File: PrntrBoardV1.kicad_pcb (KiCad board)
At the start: 4 copper layers, 99 x 99 mm, 221 parts, among them J1 EXT 5V, J10 Probe, J11 Extruder Heater, J12 Stepper, J13 Thermistor, J14 Max, J15 Min, J16 Max, J17 Min, J18 Max, J19 Min, J2 Bed Heater, J20 Stepper, J21 Stepper, J22 Stepper, J23 Stepper, J24 Probe, J25 Extruder Heater, J26 Stepper, J27 Thermistor, J28 Thermistor, J29 12-24V, J3 Z Probe, J30 Ext Motor Clock, J4 E0 Cool, J5 E0 Part, J6 E1 Cool, J7 E1 Part, J8 Always On Fan 1, J9 Always On Fan 2, U1 4078, U11 NUCLEO-64, U2 74HCT02, U3 74LVC125, U4 TMC5130, U5 TMC5130, U6 TMC5130, U7 TMC5130, U8 TMC5130

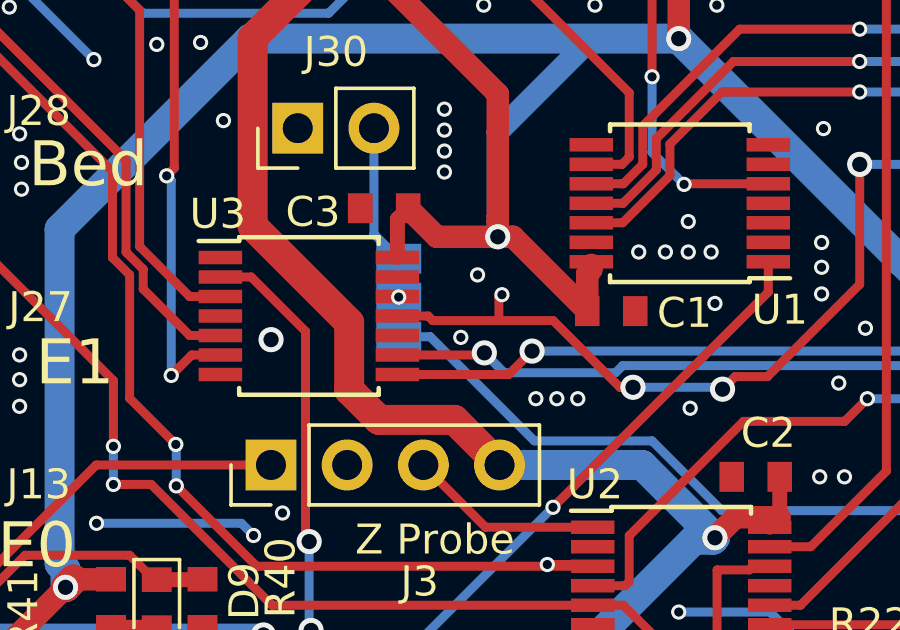
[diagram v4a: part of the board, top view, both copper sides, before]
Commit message: Some useless changes, I'll remove the SD_MODE wire soon.
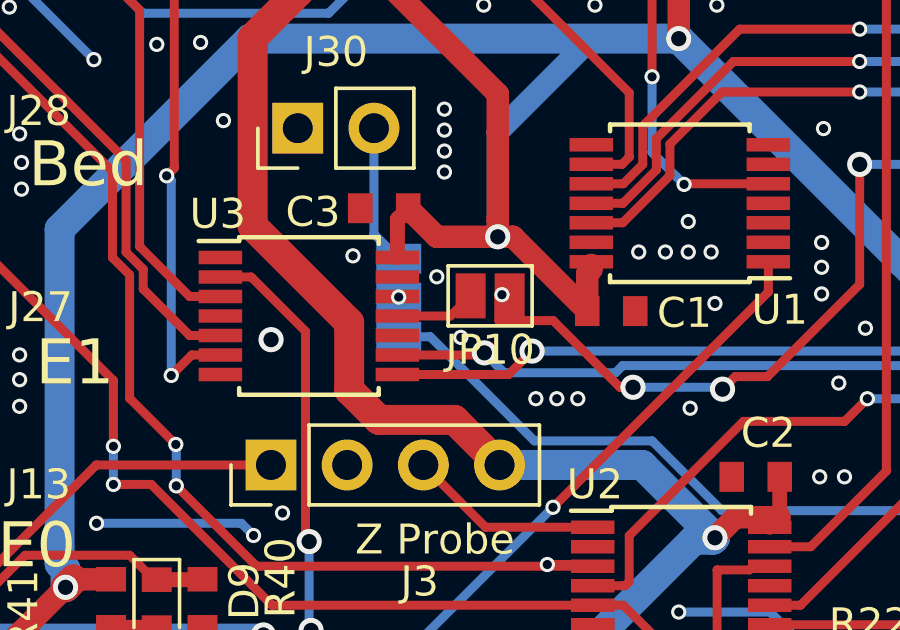
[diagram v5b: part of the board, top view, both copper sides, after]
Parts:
- added JP10: Motor Clock Enable, Jumper:SolderJumper-2_P1.3mm_Open_Pad1.0x1.5mm, F.Cu at (53.4, 75.1)
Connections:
- U3 pad 11: /MotorControl/E0/CLOCK -> Net-(JP10-Pad2)
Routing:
- net /MotorControl/E0/CLOCK: track 207.4 -> 203.9 mm
- net Net-(JP10-Pad2): track 0.00 -> 2.72 mm
- net GND: vias 681 -> 682
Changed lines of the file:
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@@
     (tracks 2655)
     (zones 0)
-    (modules 221)
-    (nets 208)
+    (modules 222)
+    (nets 209)
   )
   (page A4)
@@
   (net 206 "/MotorControl/Z Motors/Motor1/MOTB1")
   (net 207 "Net-(JP8-Pad2)")
+  (net 208 "Net-(JP10-Pad2)")
   (net_class Default "This is the default net class."
     (clearance 0.1524)
@@
     (add_net "Net-(J3-Pad1)")
     (add_net "Net-(J30-Pad2)")
+    (add_net "Net-(JP10-Pad2)")
     (add_net "Net-(JP2-Pad1)")
     (add_net "Net-(JP8-Pad2)")
@@
     (add_net /5V)
   )
+  (module Jumper:SolderJumper-2_P1.3mm_Open_Pad1.0x1.5mm (layer F.Cu)
+    (at 53.4035 75.1205 180)
+    (descr "SMD Solder Jumper, 1x1.5mm Pads, 0.3mm gap, open")
+    (tags "solder jumper open")
+    (attr virtual)
+    (fp_text reference JP10 (at 0 -1.8 180) (layer F.SilkS)
+      (effects (font (size 1 1) (thickness 0.15)))
+    )
+    (fp_text value "Motor Clock Enable" (at 0 1.9 180) (layer F.Fab)
+      (effects (font (size 1 1) (thickness 0.15)))
+    )
+    (fp_line (start -1.4 1) (end -1.4 -1) (layer F.SilkS) (width 0.12))
+    (fp_line (start 1.4 1) (end -1.4 1) (layer F.SilkS) (width 0.12))
+    (fp_line (start 1.4 -1) (end 1.4 1) (layer F.SilkS) (width 0.12))
+    (fp_line (start -1.4 -1) (end 1.4 -1) (layer F.SilkS) (width 0.12))
+    (fp_line (start -1.65 -1.25) (end 1.65 -1.25) (layer F.CrtYd) (width 0.05))
+    (fp_line (start -1.65 -1.25) (end -1.65 1.25) (layer F.CrtYd) (width 0.05))
+    (fp_line (start 1.65 1.25) (end 1.65 -1.25) (layer F.CrtYd) (width 0.05))
+    (fp_line (start 1.65 1.25) (end -1.65 1.25) (layer F.CrtYd) (width 0.05))
+    (pad 2 smd rect (at 0.65 0 180) (size 1 1.5) (layers F.Cu F.Mask)
+      (net 208 "Net-(JP10-Pad2)"))
+    (pad 1 smd rect (at -0.65 0 180) (size 1 1.5) (layers F.Cu F.Mask)
+      (net 125 /MotorControl/E0/CLOCK))
+  )
   (module Resistor_SMD:R_0603_1608Metric (layer F.Cu)
     (at 66.0145 87.4395 180)
@@
       (net 126 /MOT_CLOCK))
     (pad 11 smd rect (at 2.95 0) (size 1.45 0.45) (layers F.Cu F.Paste F.Mask)
-      (net 125 /MotorControl/E0/CLOCK))
+      (net 208 "Net-(JP10-Pad2)"))
     (pad 10 smd rect (at 2.95 0.65) (size 1.45 0.45) (layers F.Cu F.Paste F.Mask)
       (net 8 GND))
@@
   (via (at 39.243 36.449) (size 0.508) (drill 0.3048) (layers F.Cu B.Cu) (net 8))
   (via (at 40.005 37.338) (size 0.508) (drill 0.3048) (layers F.Cu B.Cu) (net 8))
-  (via (at 52.9844 74.422) (size 0.508) (drill 0.3048) (layers F.Cu B.Cu) (net 8))
   (via (at 52.4256 76.5048) (size 0.508) (drill 0.3048) (layers F.Cu B.Cu) (net 8))
   (via (at 64.516 69.5452) (size 0.508) (drill 0.3048) (layers F.Cu B.Cu) (net 8))
@@
   (via (at 67.8815 86.868) (size 0.508) (drill 0.3048) (layers F.Cu B.Cu) (net 8))
   (via (at 64.9605 90.1065) (size 0.508) (drill 0.3048) (layers F.Cu B.Cu) (net 8))
+  (via (at 51.6255 74.4855) (size 0.508) (drill 0.3048) (layers F.Cu B.Cu) (net 8))
+  (via (at 48.8315 73.787) (size 0.508) (drill 0.3048) (layers F.Cu B.Cu) (net 8))
   (segment (start 73.364029 28.9306) (end 72.794629 29.5) (width 0.5) (layer F.Cu) (net 9))
   (segment (start 75.7653 28.9306) (end 74.5 28.9306) (width 0.5) (layer F.Cu) (net 9))
@@
   (segment (start 107.394322 74.669788) (end 107.711822 74.352288) (width 0.3) (layer B.Cu) (net 125))
   (segment (start 109.03175 61.646687) (end 109.03175 56.99575) (width 0.3) (layer B.Cu) (net 125))
-  (segment (start 51.337901 75.7929) (end 51.491001 75.946) (width 0.3) (layer F.Cu) (net 125))
-  (segment (start 50.312901 75.7929) (end 51.337901 75.7929) (width 0.3) (layer F.Cu) (net 125))
   (via (at 58.166 78.1685) (size 0.8382) (drill 0.508) (layers F.Cu B.Cu) (net 125))
   (segment (start 57.727678 78.1685) (end 58.166 78.1685) (width 0.3) (layer F.Cu) (net 125))
@@
   (segment (start 107.711822 74.352288) (end 107.711822 67.945) (width 0.3) (layer B.Cu) (net 125))
   (segment (start 53.6956 75.184) (end 53.7972 75.0824) (width 0.3) (layer F.Cu) (net 125))
-  (segment (start 51.491001 75.946) (end 53.6956 75.946) (width 0.3) (layer F.Cu) (net 125))
   (via (at 53.7972 75.0824) (size 0.508) (drill 0.3048) (layers F.Cu B.Cu) (net 125))
   (segment (start 53.6956 75.946) (end 53.6956 75.184) (width 0.3) (layer F.Cu) (net 125))
@@
   (segment (start 48.314799 38.978727) (end 49.659427 37.634099) (width 0.5) (layer In1.Cu) (net 207))
   (segment (start 49.659427 37.634099) (end 54.163073 37.634099) (width 0.5) (layer In1.Cu) (net 207))
+  (segment (start 52.0811 75.7929) (end 52.7535 75.1205) (width 0.3) (layer F.Cu) (net 208))
+  (segment (start 50.312901 75.7929) (end 52.0811 75.7929) (width 0.3) (layer F.Cu) (net 208))
   (zone (net 8) (net_name GND) (layer F.Cu) (hatch edge 0.508)
     (connect_pads (clearance 0.1524))

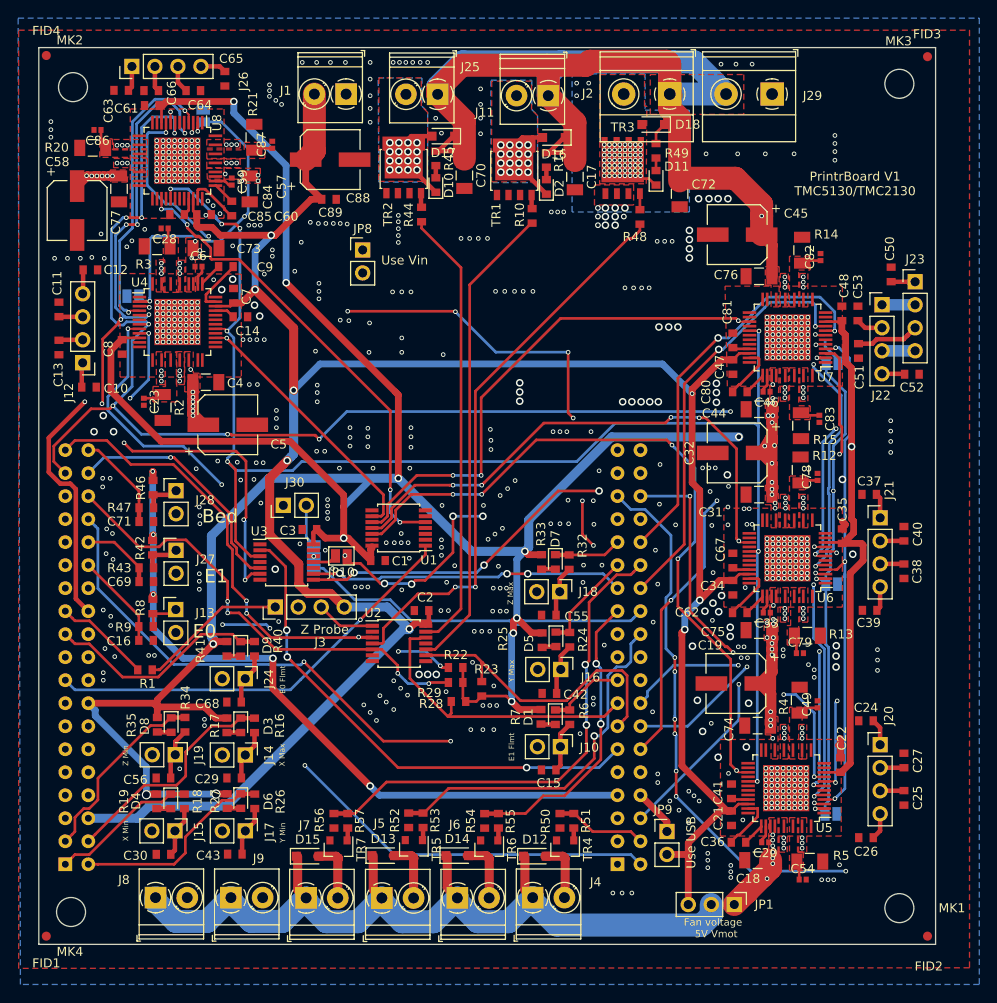
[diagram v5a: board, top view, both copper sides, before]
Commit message: Removed SD_MODE wire. Added motor clock oscillator. Wired the clock on the internal layer to reduce EMI.
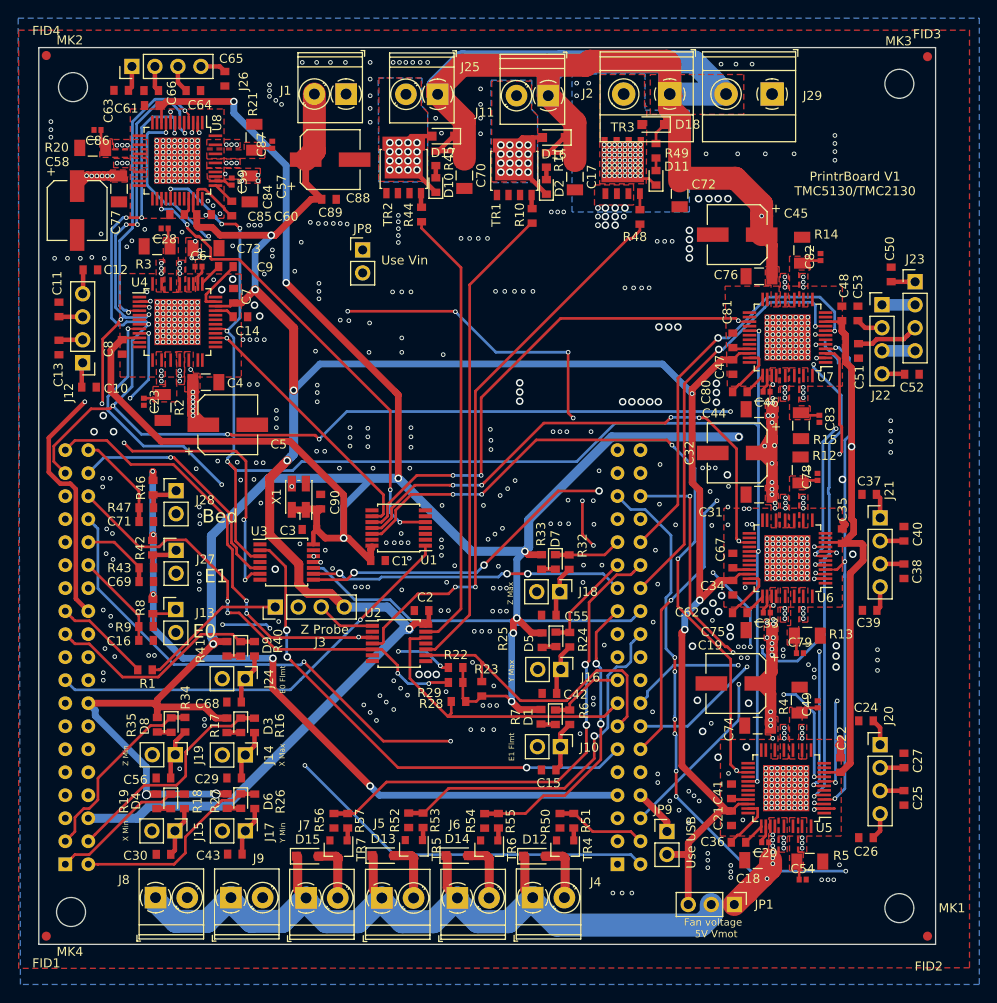
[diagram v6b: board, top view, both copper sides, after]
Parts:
- removed J30: Ext Motor Clock, Connector_PinHeader_2.54mm:PinHeader_1x02_P2.54mm_Vertical
- removed JP10: Motor Clock Enable, Jumper:SolderJumper-2_P1.3mm_Open_Pad1.0x1.5mm
- removed JP2: Motor Clock Select, Jumper:SolderJumper-3_P1.3mm_Open_Pad1.0x1.5mm
- removed JP3, JP4, JP5, JP6, JP7: Clock Disable, Jumper:SolderJumper-2_P1.3mm_Open_Pad1.0x1.5mm
- added C90: 0.1uF, Capacitor_SMD:C_0603_1608Metric, F.Cu at (51.1, 69.1)
- added X1: 16MHz, Oscillator:Oscillator_SMD_EuroQuartz_XO32-4Pin_3.2x2.5mm_HandSoldering, F.Cu at (48.7, 68.6)
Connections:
- U3 pad 11: Net-(JP10-Pad2) -> /MotorControl/E0/CLOCK
- U3 pad 12: /MOT_CLOCK -> Net-(U3-Pad12)
- U4 pad 11: GND -> Net-(U4-Pad11)
- U5 pad 11: GND -> Net-(U5-Pad11)
- U6 pad 11: GND -> Net-(U6-Pad11)
- U7 pad 11: GND -> Net-(U7-Pad11)
- U8 pad 11: GND -> Net-(U8-Pad11)
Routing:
- net /MotorControl/E0/CLOCK: track 203.9 -> 225.1 mm, vias 12 -> 6
- net /MotorControl/E0/MOSI: track 208.1 -> 218.9 mm, vias 15 -> 16
- net Net-(U3-Pad12): track 0.00 -> 8.73 mm, vias 0 -> 2
- net /3.3V: track 367.5 -> 373.2 mm
- net Net-(J30-Pad2): track 4.69 -> 0.00 mm
- net Net-(JP10-Pad2): track 2.72 -> 0.00 mm
- net /MOT_CLOCK: track 0.02 -> 0.00 mm, vias 1 -> 0
- net GND: vias 682 -> 680

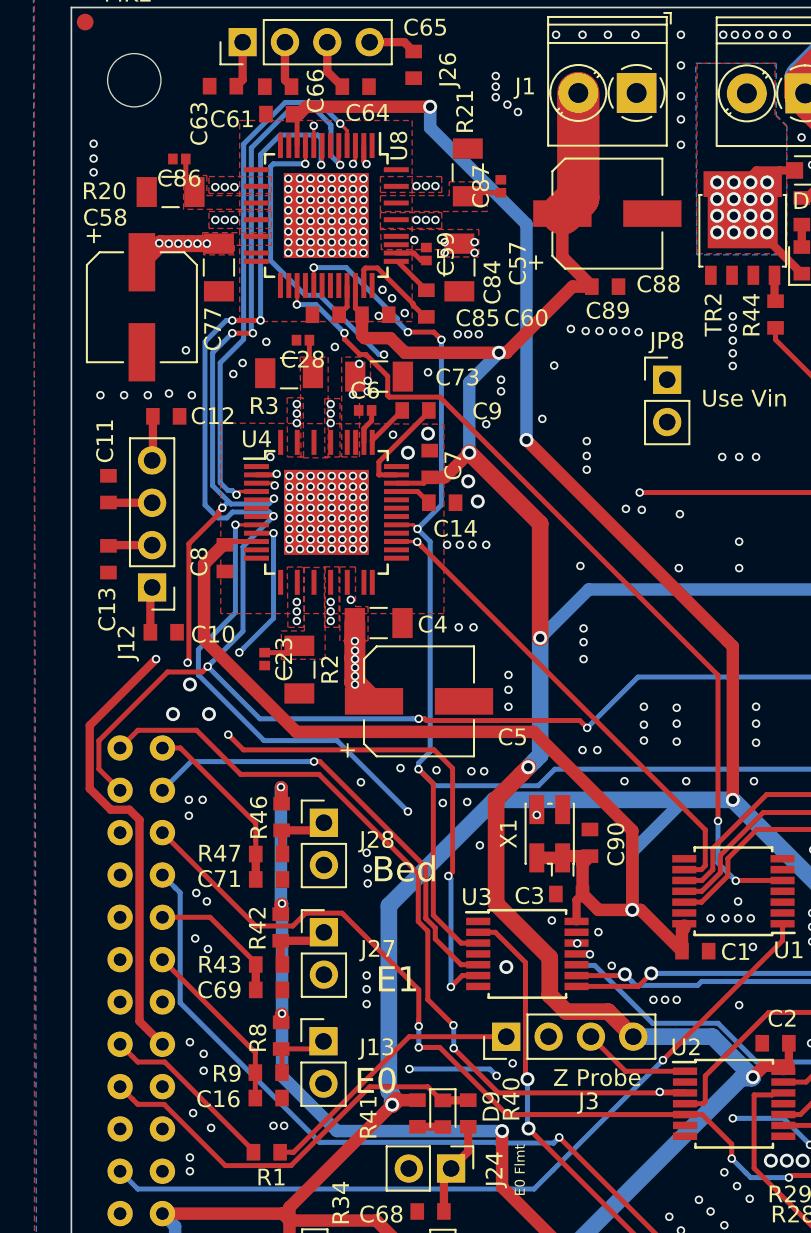
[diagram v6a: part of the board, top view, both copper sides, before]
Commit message: Re-routed the extruder motor controls, so there is a large area on the bottom to disipate the IC heat.
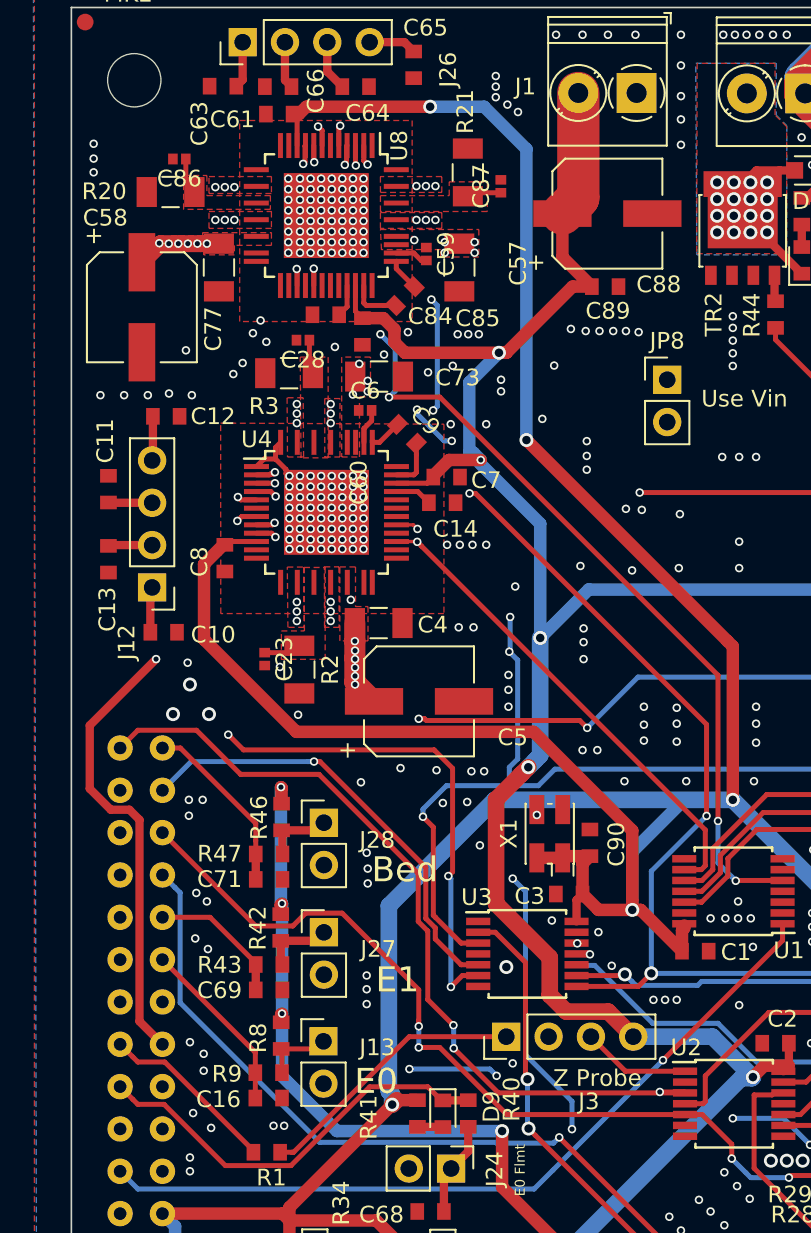
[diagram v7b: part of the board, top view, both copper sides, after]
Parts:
- moved C9 1.49 mm to (40.1, 44.6), turned to 315 degrees
- moved C84 1.37 mm to (40.0, 36.3), turned to 225 degrees
- moved C7 1.29 mm to (42.5, 47.2), turned to 180 degrees
- moved C60 1.27 mm to (37.5, 38.4), turned to 90 degrees
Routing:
- net /E0_DIR: track 99.1 -> 130.9 mm, vias 3 -> 4
- net /MotorControl/E0/SCK: track 196.6 -> 208.9 mm, vias 10 -> 14
- net /MISO: track 198.7 -> 187.7 mm, vias 13 -> 11
- net /MotorControl/E0/MOSI: track 218.9 -> 211.4 mm, vias 16 -> 14
- net Net-(JP8-Pad2): track 78.8 -> 72.7 mm, vias 2 -> 3
- net /~E0_CS: track 99.1 -> 94.1 mm, vias 3 -> 5
- net GND: track 6.61 -> 10.5 mm, vias 680 -> 671
- net Net-(C9-Pad2): track 6.16 -> 3.01 mm
- net Net-(C84-Pad2): track 6.01 -> 3.01 mm
- net /E0_STEP: track 79.0 -> 76.3 mm, vias 2 -> 1
- net /E1_STEP: track 126.0 -> 128.5 mm
- net /MotorControl/E1_SG: track 52.1 -> 54.3 mm, vias 4 -> 5
- net /3.3V: track 373.2 -> 375.1 mm
- net /5V: track 272.5 -> 273.7 mm
- net /MotorControl/E0/CLOCK: track 225.1 -> 223.9 mm, vias 6 -> 8
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
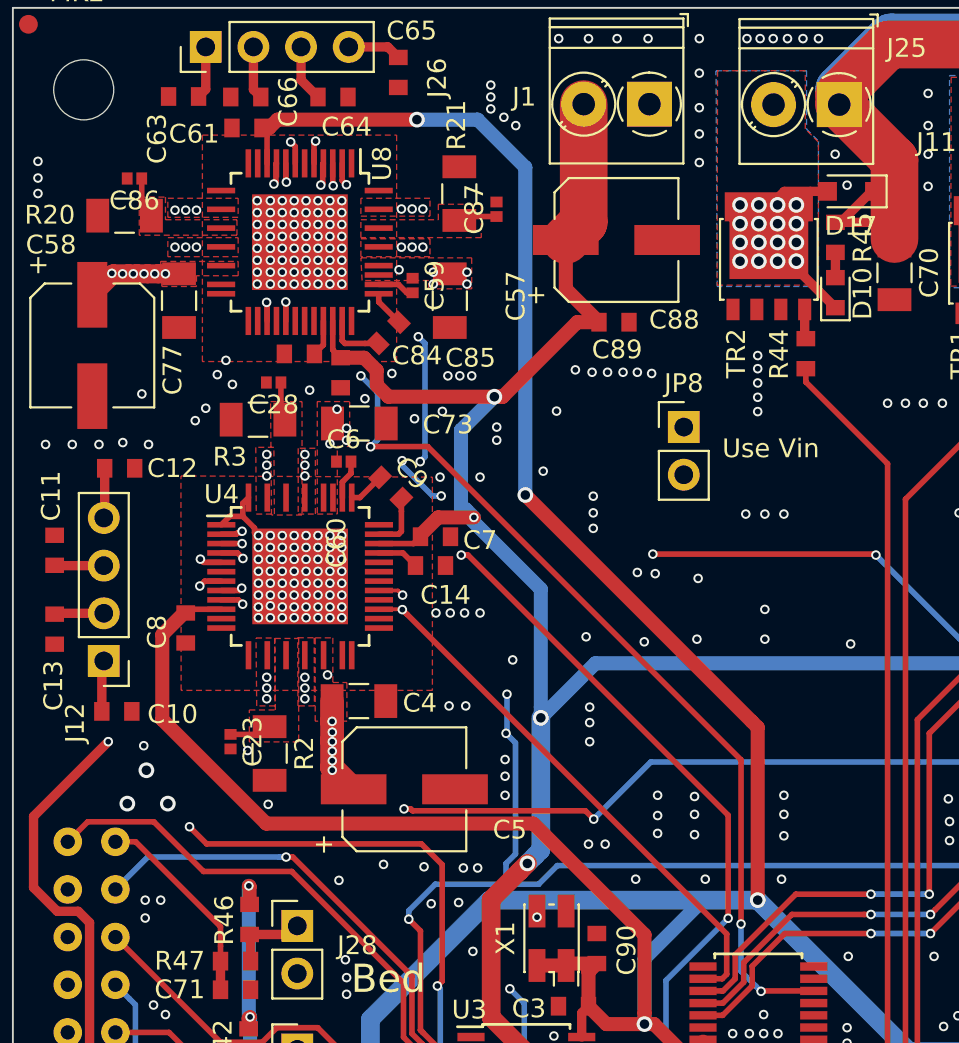
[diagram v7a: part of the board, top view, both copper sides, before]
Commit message: Remove more heat obstacles on the bottom plate.
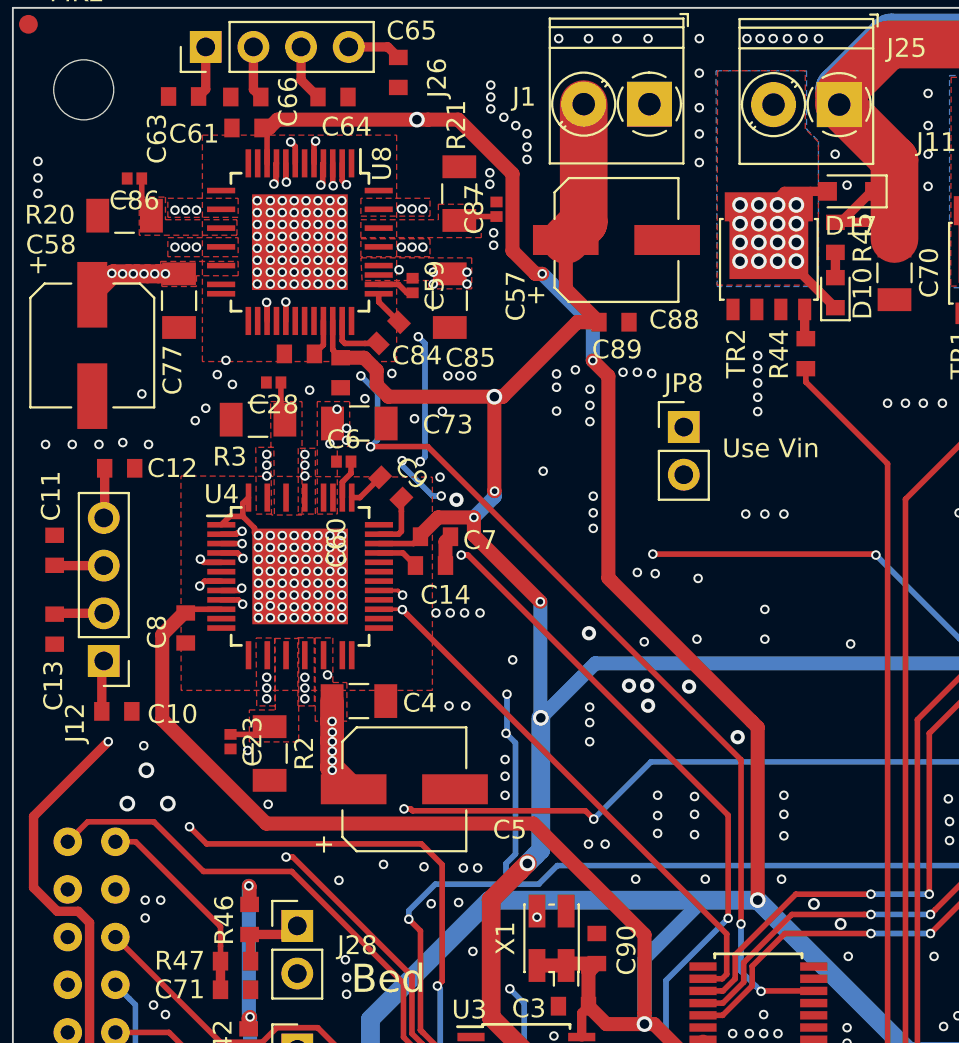
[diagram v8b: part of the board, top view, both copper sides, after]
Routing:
- net GND: track 10.5 -> 12.1 mm, vias 671 -> 685
- net /5V: track 273.7 -> 272.3 mm, vias 8 -> 10
- net /3.3V: track 375.1 -> 374.7 mm, vias 13 -> 14
- net /V_MOTORS: vias 60 -> 61
